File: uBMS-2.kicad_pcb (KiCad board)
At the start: 4 copper layers, 65 x 100 mm, 245 parts, among them J1 DX07S016JA1R1500, J2 XT60PW-M20, J3 XT60PW-M20, J5 Conn_02x07_Odd_Even, J6 Conn_02x07_Odd_Even, J7 Conn_02x07_Odd_Even, Q10 FQD5N20L, Q11 FQD5N20L, Q12 FQD5N20L, Q13 FQD5N20L, Q14 FQD5N20L, Q15 FQD5N20L, Q3 NTD5865NL, Q4 FQD5N20L, Q5 FQD5N20L, Q6 FQD5N20L, Q7 FQD5N20L, Q8 FQD5N20L, Q9 FQD5N20L, SW1 PTS815_SJK_250_SMTR_LFS, SW2 PTS815_SJK_250_SMTR_LFS, SW3 PTS815_SJK_250_SMTR_LFS, U1 ESP32-S2-MINI-1, U10 CD74HC4067SM, U11 CD74HC4067SM, U12 TXS0108EPW, U13 SN74HC595BRWNR, U2 ADS1115IDGS, U3 LM5166X, U4 TL431DBZ, U5 TLV1117-33, U6 TSC2012IDT, U7 SN74HC595BRWNR, U8 SN74HC595BRWNR, U9 VDMG10C0

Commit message: Basically Done
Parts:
- added G***: LOGO, uBMS-2:logoFP, F.Cu at (50.0, 110.1)
- moved R88 0.50 mm to (30.5, 48.6)
- moved C50 0.50 mm to (28.1, 47.9)
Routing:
- net GND: track 94.8 -> 96.2 mm
- net /VBUS: track 18.9 -> 19.7 mm
- removed copper zone on F.Cu, net /USB_D_UT+
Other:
- board text added: "Rev 2.5"

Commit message: Done V2.5
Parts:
- J1: value DX07S016JA1R1500 -> JAE_DX07S016JA1R1500
- SW1, SW2, SW3: value PTS815_SJK_250_SMTR_LFS -> SWITCH
- U1: value ESP32-S2-MINI-1 -> QFN60_ESP32-S2-MINI-1_EXP

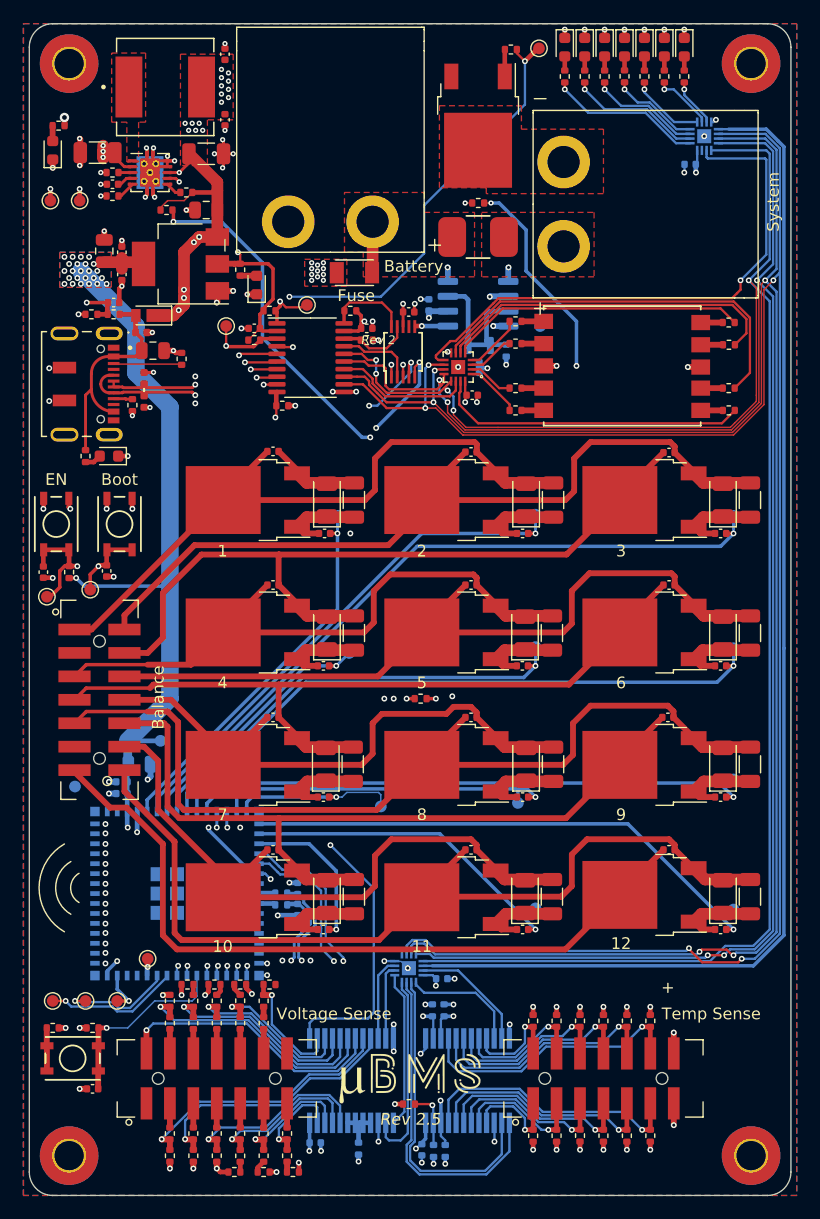
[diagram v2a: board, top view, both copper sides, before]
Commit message: Updated PCB and Gerbers for JLCPCB
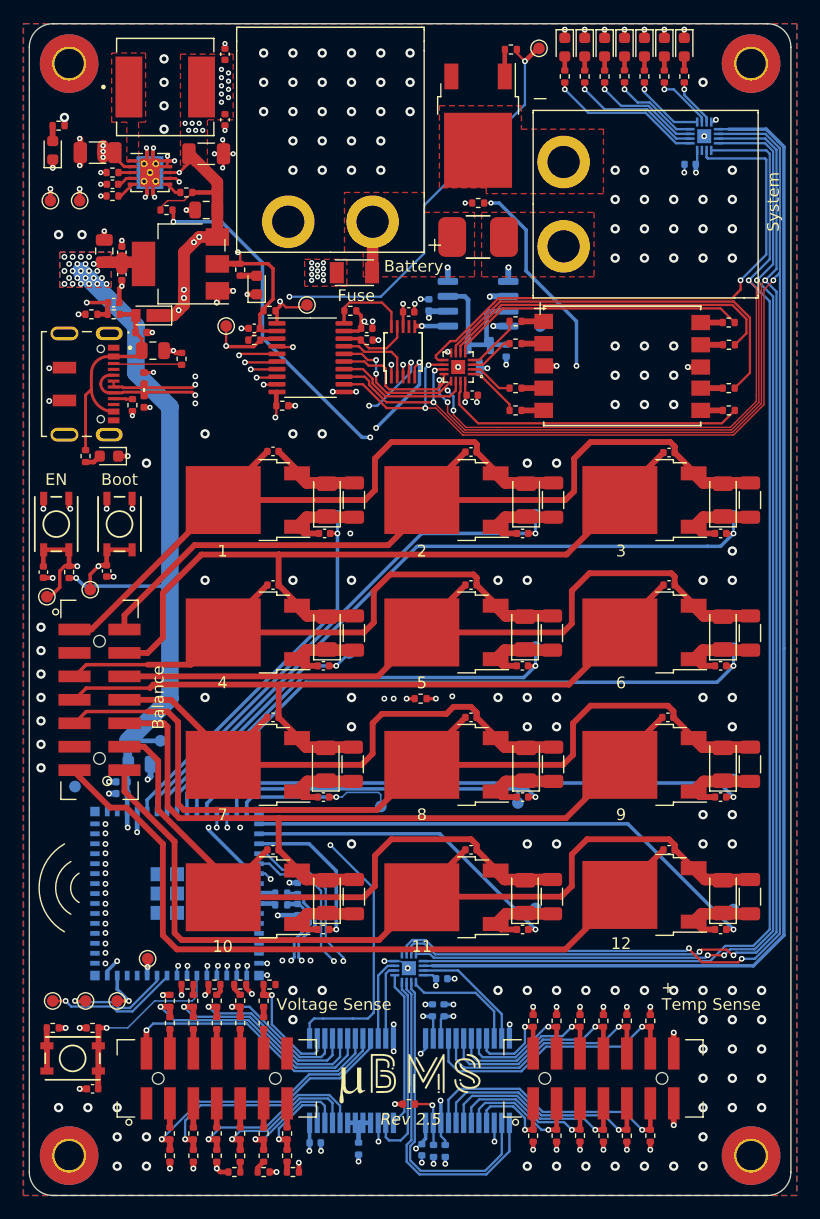
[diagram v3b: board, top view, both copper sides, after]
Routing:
- net /BatteryBalance/Cell1_P: track 57.9 -> 56.7 mm
- net /BatteryBalance/Cell8_P: track 78.9 -> 78.3 mm
- net /BatteryBalance/Cell2_P: track 71.5 -> 70.8 mm
- net GND: vias 131 -> 270
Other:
- board text removed: "Rev 2"

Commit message: Updates to layout and PCBWay Gerbers
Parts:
- moved TP24 3.73 mm to (57.3, 21.6)
- moved J2 2.40 mm to (71.5, 35.4)
- moved Q3 1.58 mm to (57.4, 28.6)
- moved R10 1.58 mm to (60.2, 22.1)
- moved R7 1.50 mm to (57.3, 38.3)
- moved TH1 1.47 mm to (57.3, 35.3)
- moved TP21 1.20 mm to (19.4, 36.3)
- moved TP23 1.20 mm to (21.9, 36.3)
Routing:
- net /MOD_DSC_G: track 89.3 -> 92.9 mm
- net /Batt_Pos: track 5.57 -> 6.82 mm
- net /SYS_Pos: track 1.21 -> 2.14 mm
- net GND: vias 270 -> 273
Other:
- board text added: "3V3"
- board text added: "5V"
- board text added: "TS"
- board text added: "USB"
- board text added: "VS"
- board text removed: "+"
- board text removed: "Temp Sense"
- board text removed: "Voltage Sense"
